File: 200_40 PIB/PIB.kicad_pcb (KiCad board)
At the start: 4 copper layers, 80 x 49 mm, 304 parts, among them J1 M80-5100442, J10 53398-0671, J11 53398-0271, J12 M80-5100842, J13 53398-0271, J15 53398-0571, J2 53398-0471, J3 G125-MS12605M2P, J4 53398-0671, J5 53398-1371, J6 MMCX, J7 MMCX, J8 SWD/DEBUG, J9 53398-0671, Q1 Si7489DP, Q10 IRF7832, Q11 IRF7832, Q2 Si7489DP, Q3 BSS138, Q4 BSS138, Q5 BSS138, Q6 Si7489DP, Q9 IRF7832, SW1 SKRKAHE020, U1 LT3065EDDPBF, U10 LT8580EDD, U11 OP27, U12 MAX823TEUK_T, U13 74LVC1G18DBV, U14 74HC08PW, U15 74HC08PW, U16 74LVC2G157DCU, U17 74LVC1G18DBV, U18 74LVC2G14, U19 ADM1270ACPZ, U2 MIC4424YM, U3 MIC4424YM, U4 STM32G431RBTx, U5 ADM1270ACPZ, U6 LM1117MP-3.3, U7 ADM1270ACPZ, U8 74AHC1G125, U9 74LVC2G17, Y1 ABM3B-8.000MHZ-10-D1G-T

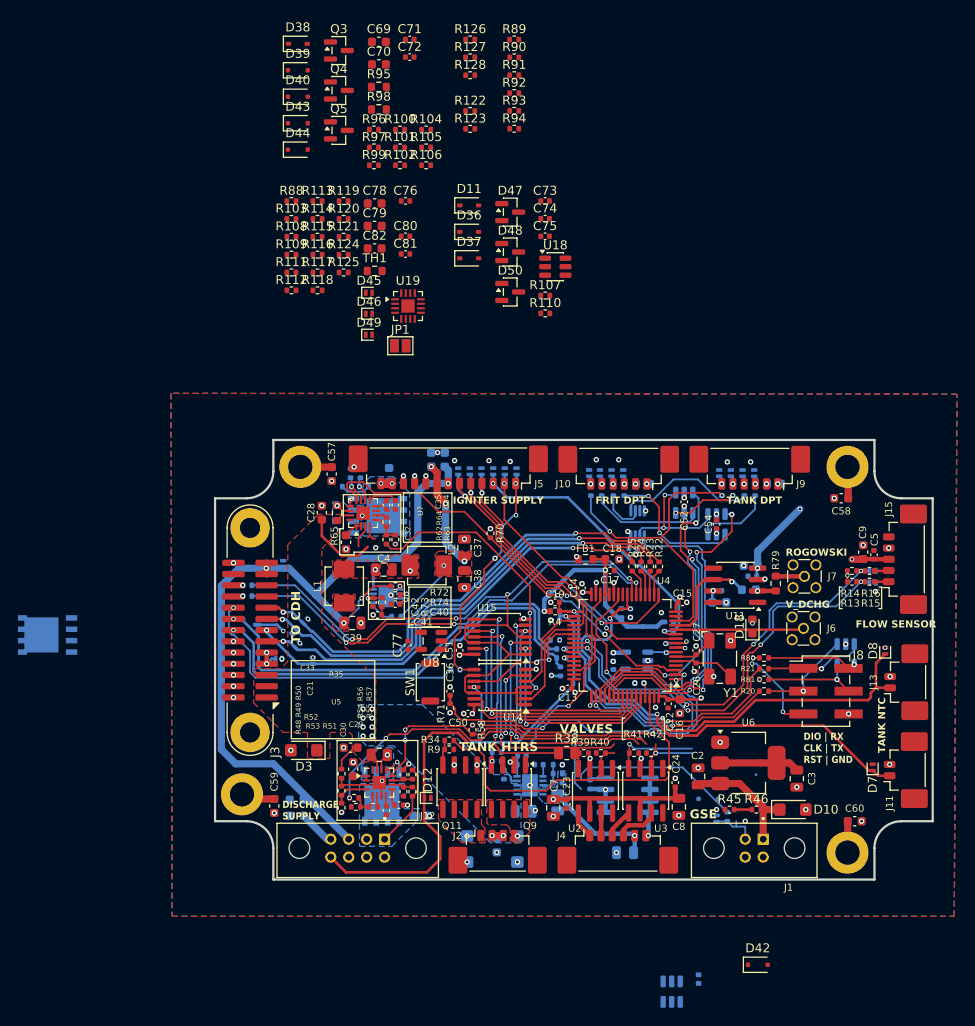
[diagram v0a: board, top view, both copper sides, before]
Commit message: finish routing with all critical schematic fixes
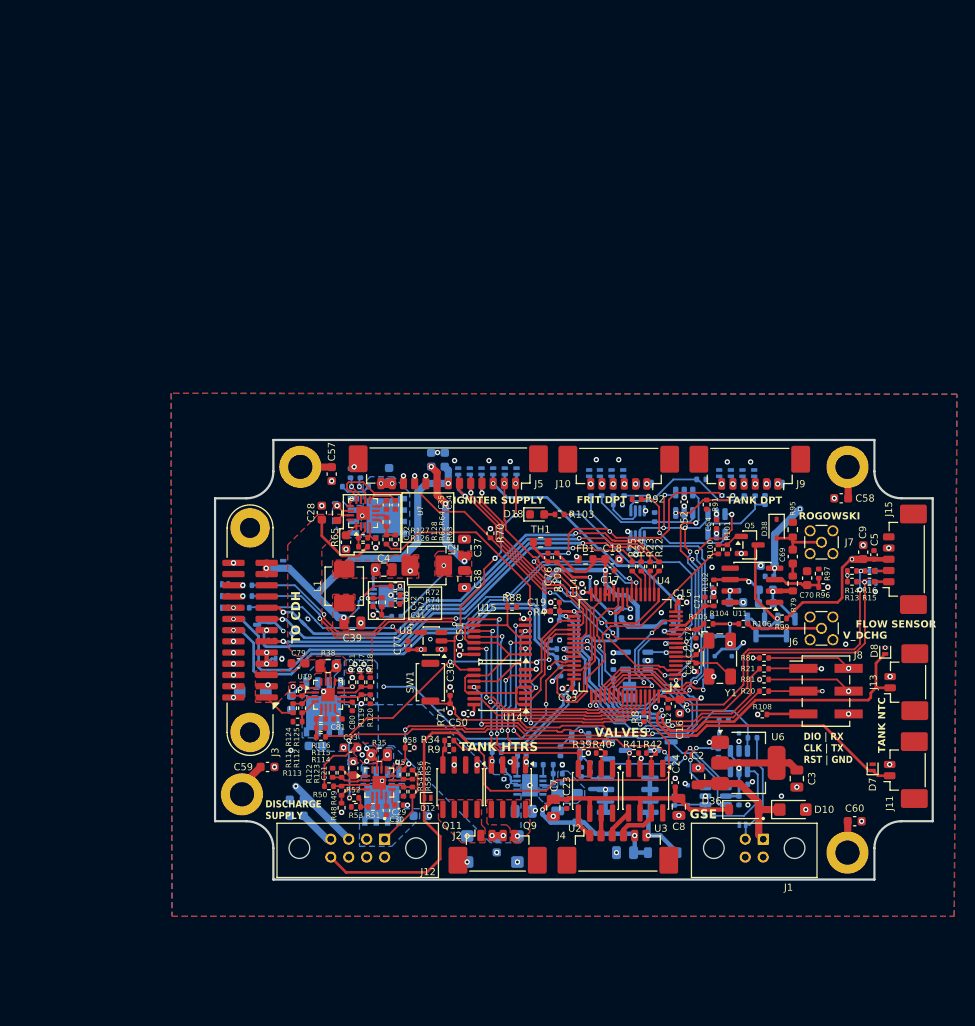
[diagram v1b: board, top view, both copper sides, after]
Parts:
- removed D17: ESDA5V3SC5, Package_TO_SOT_SMD:SOT-23-5
- added D51: PESD3V3U1UL, Diode_SMD:D_SOD-882, B.Cu at (253.0, 119.5)
- added D52: PESD3V3U1UL, Diode_SMD:D_SOD-882, B.Cu at (253.0, 117.0)
- added D53: PESD3V3U1UL, Diode_SMD:D_SOD-882, B.Cu at (256.2, 117.0)
- added D54: PESD3V3U1UL, Diode_SMD:D_SOD-882, B.Cu at (256.2, 119.5)
- C73, C74, C75, C78, C82, D3, D39, D40, D42, D43, D44, D45, D46, D47, D48, D49, D50, JP1, R107, R110, R45, R46, R89, R90, R93, R94, R98, U18: moved to B.Cu
- D11, D37: value NSVR1020MW2T1G -> MBR0560; footprint Diode_SMD:D_SOD-323 -> Diode_SMD:D_SOD-123; moved to B.Cu
- D36: value NSVR1020MW2T1G -> MBR0560; footprint Diode_SMD:D_SOD-323 -> Diode_SMD:D_SOD-123
- Q3, Q4: value BSS138 -> BSS131; moved to B.Cu
- Q5: value BSS138 -> BSS131
- R8: moved to F.Cu
- moved Q3 79.4 mm to (246.8, 112.4), turned to -90 degrees
- moved Q4 77.9 mm to (250.2, 112.4), turned to -90 degrees
- moved D38 76.0 mm to (249.1, 101.4), turned to -90 degrees
- moved D39 75.6 mm to (241.9, 110.1), turned to -90 degrees
- moved R122 75.3 mm to (199.6, 128.6), turned to -90 degrees
- moved R108 74.8 mm to (247.5, 122.1)
- moved D43 74.6 mm to (242.2, 114.5), turned to 90 degrees
- moved C70 74.6 mm to (252.5, 106.9), turned to 90 degrees
- moved C69 73.6 mm to (250.9, 104.5), turned to -90 degrees
- moved D44 73.5 mm to (244.1, 114.5), turned to -90 degrees
- moved R123 73.2 mm to (200.6, 128.6), turned to 90 degrees
- moved C72 71.8 mm to (240.1, 113.1), turned to -90 degrees
- moved R96 71.5 mm to (254.3, 107.9), turned to 180 degrees
- moved D36 71.3 mm to (245.4, 132.7)
- moved C71 70.8 mm to (241.1, 109.5), turned to 90 degrees
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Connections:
- R96 pad 1: VDDA -> +3.3V
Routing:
- net /DPT_MCLK: track 0.00 -> 46.0 mm, vias 0 -> 4
- net (no net): track 41.5 -> 0.00 mm, vias 2 -> 0
- net /DEBUG_LED: track 0.00 -> 38.9 mm, vias 0 -> 2
- net /BAT_PGOOD: track 0.00 -> 34.0 mm, vias 0 -> 3
- net /~{PD_RST}: track 27.5 -> 60.3 mm
- net /BAT_EN: track 0.00 -> 32.5 mm, vias 0 -> 3
- net /12V_PG: track 2.14 -> 33.4 mm, vias 0 -> 3
- net Net-(D45-K): track 31.5 -> 1.24 mm
- net /Valve Driver/EGSE_OPEN_F: track 0.00 -> 27.4 mm
- net /IGNITER_EXT: track 0.00 -> 20.5 mm, vias 0 -> 1
- net /nRST: track 22.7 -> 3.18 mm, vias 3 -> 1
- net Net-(Q10-G): track 22.1 -> 3.30 mm
- net Net-(D47-Pad1): track 0.00 -> 16.4 mm, vias 0 -> 2
- net /ADC_NTC_PIB: track 0.00 -> 16.3 mm, vias 0 -> 2
- net Net-(Q3-G): track 0.00 -> 13.9 mm, vias 0 -> 1
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- added copper zone on B.Cu, net Net-(D11-A)
- added copper zone on B.Cu, net Net-(U19-SENSE-)
- added copper zone on F.Cu, net VBAT_PROT
- removed copper zone on B.Cu, net +12V

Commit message: correct V igniter and I igniter pinouts and note capacitance limits from current limit timer
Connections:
- D24 pad 1: /ADC_I_IGN_PK -> /ADC_V_IGN_PK
- D25 pad 1: /ADC_V_IGN_PK -> /ADC_I_IGN_PK
- J5 pad 4: /ADC_I_IGN_PK -> /ADC_V_IGN_PK
- J5 pad 5: /ADC_V_IGN_PK -> /ADC_I_IGN_PK
- U4 pad 10: /ADC_I_IGN_PK -> /ADC_V_IGN_PK
- U4 pad 36: /ADC_V_IGN_PK -> /ADC_I_IGN_PK
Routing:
- net /ADC_V_IGN_PK: track 25.0 -> 33.6 mm, vias 1 -> 3
- net /ADC_I_IGN_PK: track 33.6 -> 25.0 mm, vias 3 -> 1

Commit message: add uvlo to gse valve drive
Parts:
- added D17: BAT54J, Diode_SMD:D_SOD-323F, B.Cu at (213.8, 102.9)
- added D55: BAT54J, Diode_SMD:D_SOD-323F, B.Cu at (213.8, 99.7)
- added D56: BAT54J, Diode_SMD:D_SOD-323F, B.Cu at (218.3, 101.4)
- added D57: BAT54J, Diode_SMD:D_SOD-323F, B.Cu at (218.3, 99.5)
- added D58: BAT54J, Diode_SMD:D_SOD-323F, B.Cu at (215.7, 99.7)
- added D59: BAT54J, Diode_SMD:D_SOD-323F, B.Cu at (215.7, 102.9)
- added R129: 1K, Resistor_SMD:R_0402_1005Metric, F.Cu at (214.3, 99.2)
- added R130: 1K, Resistor_SMD:R_0402_1005Metric, F.Cu at (216.3, 99.2)
- added R131: 1K, Resistor_SMD:R_0402_1005Metric, F.Cu at (215.3, 99.2)
- C35: value 10nF -> 68nF
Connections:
- U4 pad 10: /ADC_V_IGN_PK -> /ADC_V_IGN_PK_C
- U4 pad 17: /ADC_V_IGN_SUPPLY -> /ADC_V_IGN_SUPPLY_C
- U4 pad 36: /ADC_I_IGN_PK -> /ADC_I_IGN_PK_C
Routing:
- net /ADC_V_IGN_PK_C: track 0.00 -> 32.4 mm, vias 0 -> 3
- net /ADC_V_IGN_SUPPLY_C: track 0.00 -> 31.4 mm, vias 0 -> 3
- net /ADC_V_IGN_PK: track 33.6 -> 4.43 mm, vias 3 -> 1
- net /ADC_V_IGN_SUPPLY: track 34.7 -> 6.37 mm, vias 3 -> 1
- net /ADC_I_IGN_PK_C: track 0.00 -> 22.5 mm, vias 0 -> 1
- net /ADC_I_IGN_PK: track 25.0 -> 4.55 mm
- net +3.3V: track 28.9 -> 34.2 mm
- net -5V: track 137.7 -> 138.3 mm
- net GND: vias 117 -> 118

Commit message: review items closed out
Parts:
- added R43: 1.5K, Resistor_SMD:R_0402_1005Metric, F.Cu at (251.3, 126.3)
- added R44: 12.1K, Resistor_SMD:R_0402_1005Metric, F.Cu at (251.3, 127.3)
- U6: value LM1117MP-3.3 -> ADP7142AUJZ-3.3; footprint Package_TO_SOT_SMD:SOT-223-3_TabPin2 -> Package_TO_SOT_SMD:TSOT-23-5
- moved C2 11.1 mm to (251.4, 129.6)
- moved C3 4.04 mm to (248.1, 126.8), turned to 0 degrees
- moved U6 3.16 mm to (248.3, 129.6), turned to 180 degrees
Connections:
- U6 pad 1: GND -> 12V_GSE
- U6 pad 2: 3.3V_EGSE -> GND
- U6 pad 3: 12V_GSE -> Net-(U6-EN)
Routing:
- net 3.3V_EGSE: track 14.1 -> 10.8 mm
- net Net-(U6-EN): track 0.00 -> 2.97 mm
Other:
- board text added: "GSE VALVE OVERRIDE"
- board text removed: "GSE"
